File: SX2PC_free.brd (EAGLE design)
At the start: 20.3 x 26.8 mm, 5 parts

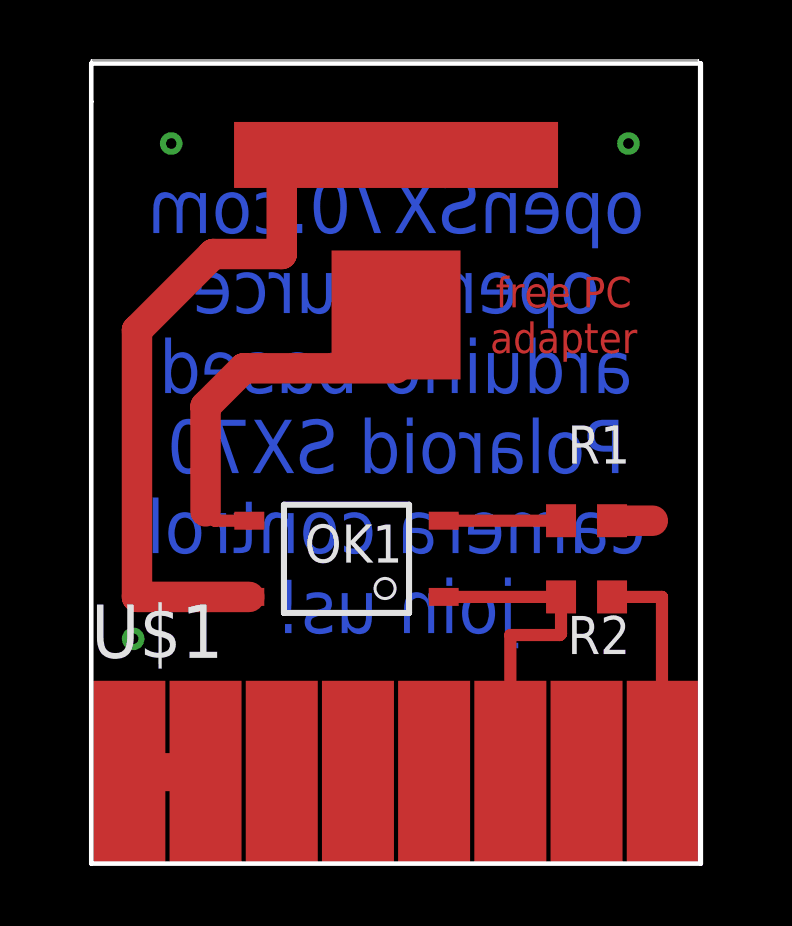
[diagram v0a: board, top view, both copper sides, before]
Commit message: Build a prototype and checked operation. Now working. Version 2.0
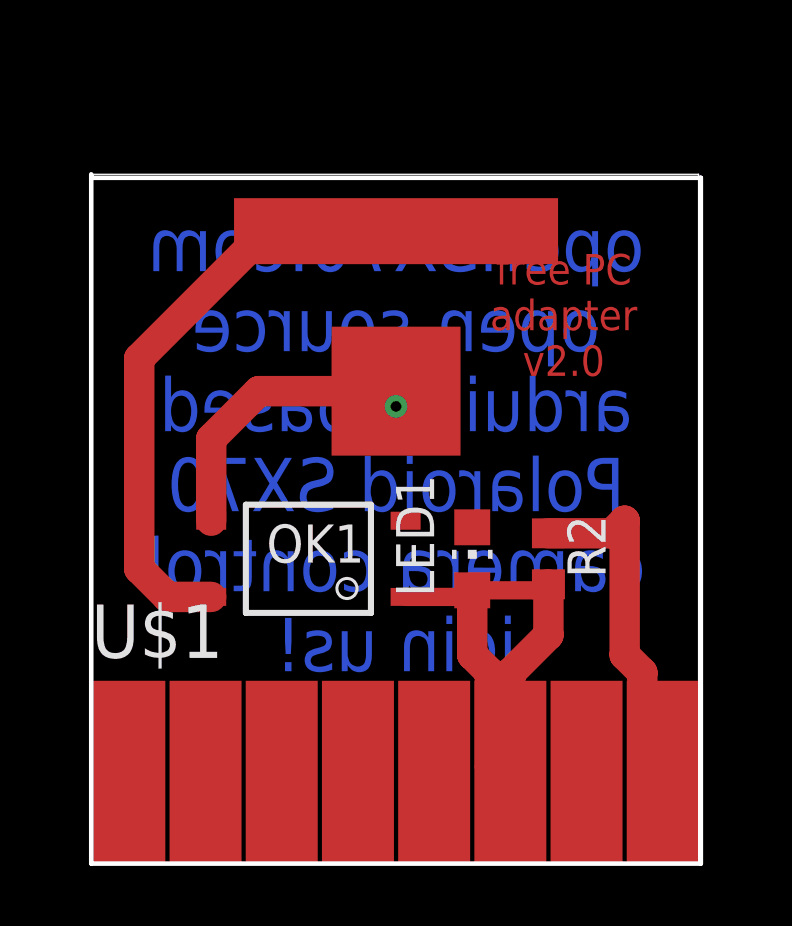
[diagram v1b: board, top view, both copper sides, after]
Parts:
- removed R1: 18R, rcl:R0603
- added LED1: (no value), led:CHIP-LED0805
- moved U$2 2.54 mm to (10.2, 19.1)
- moved R2 1.80 mm to (15.2, 10.2), turned to 90 degrees
- moved OK1 1.27 mm to (7.24, 9.53)
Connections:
- removed net N$2: OK1.2, R1.1
- net GND: now also LED1.C, OK1.2; no longer R1.2
- net N$3: now also LED1.A
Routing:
- net N$3: track 11.4 -> 19.2 mm
- net N$4: track 13.7 -> 9.55 mm
- net N$2: track 3.91 -> 0.00 mm
- net GND: track 8.87 -> 11.6 mm, vias 3 -> 0
- net N$1: track 2.54 -> 0.00 mm
- net N$5: track 25.2 -> 22.8 mm
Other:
- board size 20.3 x 26.8 mm -> 20.3 x 23 mm
- board text added: "free PC adapter v2.0"
- board text removed: "free PC adapter"
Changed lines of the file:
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@@
 <plain>
 <wire x1="0" y1="0" x2="20.244" y2="0" width="0" layer="20"/>
-<wire x1="20.244" y1="0" x2="20.244" y2="26.787" width="0" layer="20"/>
-<wire x1="20.244" y1="26.787" x2="0" y2="26.787" width="0" layer="20"/>
-<wire x1="0" y1="26.787" x2="0" y2="26.67" width="0" layer="20"/>
-<text x="10.16" y="15.24" size="1.778" layer="16" font="vector" ratio="16" rot="MR0" align="center">openSX70.com
+<wire x1="20.244" y1="0" x2="20.244" y2="22.977" width="0" layer="20"/>
+<wire x1="20.244" y1="22.977" x2="0" y2="22.977" width="0" layer="20"/>
+<text x="10.16" y="13.97" size="1.778" layer="16" font="vector" ratio="16" rot="MR0" align="center">openSX70.com
 open-source
 arduino-based
@@
 join us!</text>
 <text x="15.748" y="18.288" size="1.016" layer="1" font="vector" ratio="16" align="center">free PC
-adapter</text>
-<wire x1="0" y1="25.4" x2="0" y2="0" width="0.1524" layer="20"/>
+adapter
+v2.0</text>
+<wire x1="0" y1="22.977" x2="0" y2="22.86" width="0.1524" layer="20"/>
+<wire x1="0" y1="22.86" x2="0" y2="0" width="0.1524" layer="20"/>
 <wire x1="0" y1="0" x2="20.32" y2="0" width="0.1524" layer="20"/>
-<wire x1="20.32" y1="0" x2="20.32" y2="26.67" width="0.1524" layer="20"/>
-<wire x1="20.32" y1="26.67" x2="0" y2="26.67" width="0.1524" layer="20"/>
-<wire x1="0" y1="26.67" x2="0" y2="25.4" width="0.1524" layer="20"/>
+<wire x1="20.32" y1="0" x2="20.32" y2="22.86" width="0.1524" layer="20"/>
+<wire x1="20.32" y1="22.86" x2="0" y2="22.86" width="0.1524" layer="20"/>
 </plain>
 <attributes>
@@
 </autorouter>
 <elements>
-<element name="OK1" library="openSX70" package="SO-4" value="TLP127" x="8.509" y="9.525" smashed="yes" rot="R180">
-<attribute name="NAME" x="7.112" y="10.033" size="1.27" layer="25" font="vector" ratio="10"/>
-<attribute name="VALUE" x="5.588" y="12.446" size="1.27" layer="27" font="vector" ratio="10"/>
-</element>
-<element name="R1" library="rcl" library_urn="urn:adsk.eagle:library:334" package="R0603" package3d_urn="urn:adsk.eagle:package:23555/2" value="18R" x="16.51" y="11.43" smashed="yes">
-<attribute name="NAME" x="15.875" y="13.335" size="1.27" layer="25" font="vector"/>
-<attribute name="VALUE" x="18.415" y="10.795" size="1.27" layer="27"/>
+<element name="OK1" library="openSX70" package="SO-4" value="TLP127" x="7.239" y="9.525" smashed="yes" rot="R180">
+<attribute name="NAME" x="5.842" y="10.033" size="1.27" layer="25" font="vector" ratio="10"/>
+<attribute name="VALUE" x="4.318" y="12.446" size="1.27" layer="27" font="vector" ratio="10"/>
 </element>
 <element name="U$1" library="openSX70" package="SX70-FLASH-EDGE8" value="SX70-FLASH-EDGE8-MALE" x="10.16" y="3.048"/>
-<element name="U$2" library="openSX70" package="PC-SOCKET-KAISER-1311" value="PC-SOCKET-KAISER-1311" x="10.16" y="21.59"/>
-<element name="R2" library="rcl" library_urn="urn:adsk.eagle:library:334" package="R0603" package3d_urn="urn:adsk.eagle:package:23555/2" value="9R" x="16.51" y="8.89" smashed="yes">
-<attribute name="NAME" x="15.875" y="6.985" size="1.27" layer="25" font="vector"/>
-<attribute name="VALUE" x="18.415" y="8.255" size="1.27" layer="27" font="vector"/>
+<element name="U$2" library="openSX70" package="PC-SOCKET-KAISER-1311" value="PC-SOCKET-KAISER-1311" x="10.16" y="19.05"/>
+<element name="R2" library="rcl" library_urn="urn:adsk.eagle:library:334" package="R0603" package3d_urn="urn:adsk.eagle:package:23555/2" value="9R" x="15.24" y="10.16" smashed="yes" rot="R90">
+<attribute name="NAME" x="17.145" y="9.525" size="1.27" layer="25" font="vector" rot="R90"/>
+<attribute name="VALUE" x="15.875" y="12.065" size="1.27" layer="27" font="vector" rot="R90"/>
 </element>
+<element name="LED1" library="led" library_urn="urn:adsk.eagle:library:259" package="CHIP-LED0805" package3d_urn="urn:adsk.eagle:package:15818/1" value="" x="12.7" y="10.16"/>
 </elements>
 <signals>
@@
 <contactref element="U$1" pad="GND"/>
 <contactref element="U$1" pad="S2"/>
-<wire x1="1.27" y1="3.04926875" x2="3.81" y2="3.04926875" width="1.27" layer="1"/>
-</signal>
-<signal name="N$2">
-<contactref element="OK1" pad="2"/>
-<contactref element="R1" pad="1"/>
-<wire x1="11.749" y1="11.43" x2="15.66" y2="11.43" width="0.4064" layer="1"/>
+<wire x1="1.27" y1="3.04926875" x2="3.81" y2="3.04926875" width="0" layer="19" extent="1-1"/>
 </signal>
 <signal name="N$4">
 <contactref element="U$2" pad="TIP"/>
 <contactref element="OK1" pad="3"/>
-<wire x1="3.81" y1="15.24" x2="3.81" y2="11.74" width="1.016" layer="1"/>
-<wire x1="3.81" y1="15.24" x2="5.08" y2="16.51" width="1.016" layer="1"/>
-<wire x1="5.08" y1="16.51" x2="10.16" y2="16.51" width="1.016" layer="1"/>
-<wire x1="3.81" y1="11.74" x2="4.12" y2="11.43" width="0.4064" layer="1"/>
-<wire x1="4.12" y1="11.43" x2="5.269" y2="11.43" width="0.4064" layer="1"/>
-<wire x1="10.16" y1="16.51" x2="10.16" y2="18.288" width="0.4064" layer="1"/>
+<wire x1="3.999" y1="11.43" x2="3.999" y2="14.159" width="1.016" layer="1"/>
+<wire x1="5.588" y1="15.748" x2="10.16" y2="15.748" width="1.016" layer="1"/>
+<wire x1="3.999" y1="14.159" x2="5.588" y2="15.748" width="1.016" layer="1"/>
 </signal>
 <signal name="N$5">
 <contactref element="OK1" pad="4"/>
 <contactref element="U$2" pad="RING"/>
-<wire x1="5.269" y1="8.89" x2="1.524" y2="8.89" width="1.016" layer="1"/>
-<wire x1="1.524" y1="8.89" x2="1.524" y2="17.78" width="1.016" layer="1"/>
-<wire x1="1.524" y1="17.78" x2="4.064" y2="20.32" width="1.016" layer="1"/>
-<wire x1="4.064" y1="20.32" x2="6.35" y2="20.32" width="1.016" layer="1"/>
-<wire x1="6.35" y1="20.32" x2="6.35" y2="22.86" width="1.016" layer="1"/>
-<wire x1="6.35" y1="22.86" x2="7.112" y2="23.622" width="1.016" layer="1"/>
-<wire x1="7.112" y1="23.622" x2="10.16" y2="23.622" width="1.016" layer="1"/>
+<wire x1="3.999" y1="8.89" x2="2.54" y2="8.89" width="1.016" layer="1"/>
+<wire x1="2.54" y1="8.89" x2="1.6002" y2="9.8298" width="1.016" layer="1"/>
+<wire x1="6.0198" y1="21.2598" x2="11.43" y2="21.2598" width="1.016" layer="1"/>
+<wire x1="11.43" y1="21.2598" x2="11.2522" y2="21.082" width="1.016" layer="1"/>
+<wire x1="11.2522" y1="21.082" x2="10.16" y2="21.082" width="1.016" layer="1"/>
+<wire x1="1.6002" y1="9.8298" x2="1.6002" y2="16.8402" width="1.016" layer="1"/>
+<wire x1="1.6002" y1="16.8402" x2="6.0198" y2="21.2598" width="1.016" layer="1"/>
 </signal>
 <signal name="GND">
 <polygon width="0.508" layer="1" isolate="0.254">
-<vertex x="0" y="26.67"/>
-<vertex x="20.32" y="26.67"/>
+<vertex x="0" y="22.86"/>
+<vertex x="20.32" y="22.86"/>
 <vertex x="20.32" y="0"/>
 <vertex x="0" y="0"/>
 </polygon>
-<contactref element="R1" pad="2"/>
 <contactref element="U$1" pad="FLASH-1"/>
 <contactref element="R2" pad="2"/>
-<wire x1="17.36" y1="11.43" x2="18.72" y2="11.43" width="1.016" layer="1"/>
-<wire x1="17.36" y1="8.89" x2="19.0248" y2="8.89" width="0.4064" layer="1"/>
-<wire x1="19.0248" y1="8.89" x2="19.0248" y2="3.04926875" width="0.4064" layer="1"/>
-<via x="2.667" y="24.003" extent="1-16" drill="0.35"/>
 <polygon width="0.4064" layer="16">
-<vertex x="20.32" y="26.67"/>
+<vertex x="20.32" y="22.86"/>
 <vertex x="20.32" y="0"/>
 <vertex x="0" y="0"/>
-<vertex x="0" y="26.67"/>
+<vertex x="0" y="22.86"/>
 </polygon>
-<via x="1.397" y="7.493" extent="1-16" drill="0.35"/>
-<wire x1="19.0248" y1="3.04926875" x2="19.049996875" y2="3.04926875" width="0" layer="19" extent="1-1"/>
-<via x="17.907" y="24.003" extent="1-16" drill="0.35"/>
+<contactref element="OK1" pad="2"/>
+<contactref element="LED1" pad="C"/>
+<wire x1="15.24" y1="11.01" x2="17.36" y2="11.01" width="1.016" layer="1"/>
+<wire x1="17.36" y1="11.01" x2="17.78" y2="11.43" width="1.016" layer="1"/>
+<wire x1="18.3704" y1="6.3678125" x2="18.3704" y2="5.7596" width="1.016" layer="1"/>
+<wire x1="18.3704" y1="5.7596" x2="18.7198" y2="5.4102" width="1.016" layer="1"/>
+<wire x1="17.78" y1="11.43" x2="17.78" y2="6.9582125" width="1.016" layer="1"/>
+<wire x1="17.78" y1="6.9582125" x2="18.3704" y2="6.3678125" width="1.016" layer="1"/>
+<wire x1="18.7198" y1="5.4102" x2="18.7198" y2="3.379465625" width="1.016" layer="1"/>
+<wire x1="18.7198" y1="3.379465625" x2="19.049996875" y2="3.04926875" width="1.016" layer="1"/>
 </signal>
 <signal name="N$3">
@@
 <contactref element="U$1" pad="VCC-6V"/>
 <contactref element="R2" pad="1"/>
-<wire x1="11.749" y1="8.89" x2="15.66" y2="8.89" width="0.4064" layer="1"/>
-<wire x1="15.66" y1="8.89" x2="15.66" y2="7.659" width="0.4064" layer="1"/>
-<wire x1="15.66" y1="7.659" x2="15.621" y2="7.62" width="0.4064" layer="1"/>
-<wire x1="15.621" y1="7.62" x2="13.97" y2="7.62" width="0.4064" layer="1"/>
-<wire x1="13.97" y1="7.62" x2="13.97" y2="3.04926875" width="0.4064" layer="1"/>
+<contactref element="LED1" pad="A"/>
+<wire x1="15.24" y1="9.31" x2="15.24" y2="7.62" width="1.016" layer="1"/>
+<wire x1="15.24" y1="7.62" x2="13.97" y2="6.35" width="1.016" layer="1"/>
+<wire x1="13.97" y1="6.35" x2="13.97" y2="2.54" width="1.016" layer="1"/>
+<wire x1="13.97" y1="2.54" x2="13.2904" y2="3.2196" width="1.016" layer="1"/>
+<wire x1="13.2904" y1="3.2196" x2="13.2904" y2="6.3678125" width="1.016" layer="1"/>
+<wire x1="12.7" y1="8.89" x2="12.7" y2="6.9582125" width="1.016" layer="1"/>
+<wire x1="12.7" y1="8.89" x2="12.7" y2="9.11" width="1.016" layer="1"/>
+<wire x1="13.2904" y1="6.3678125" x2="12.7" y2="6.9582125" width="1.016" layer="1"/>
+<wire x1="10.479" y1="8.89" x2="12.7" y2="8.89" width="0.6096" layer="1"/>
+<wire x1="12.7" y1="9.11" x2="15.04" y2="9.11" width="0.6096" layer="1"/>
+<wire x1="15.04" y1="9.11" x2="15.24" y2="9.31" width="0.6096" layer="1"/>
+<wire x1="13.97" y1="2.54" x2="13.97" y2="3.04926875" width="0" layer="19" extent="1-1"/>
+</signal>
+<signal name="N$6">
+<via x="10.16" y="15.24" extent="1-16" drill="0.35" shape="square"/>
 </signal>
 </signals>

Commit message: Connected F1 and F5 to VCC or it doesn't work!
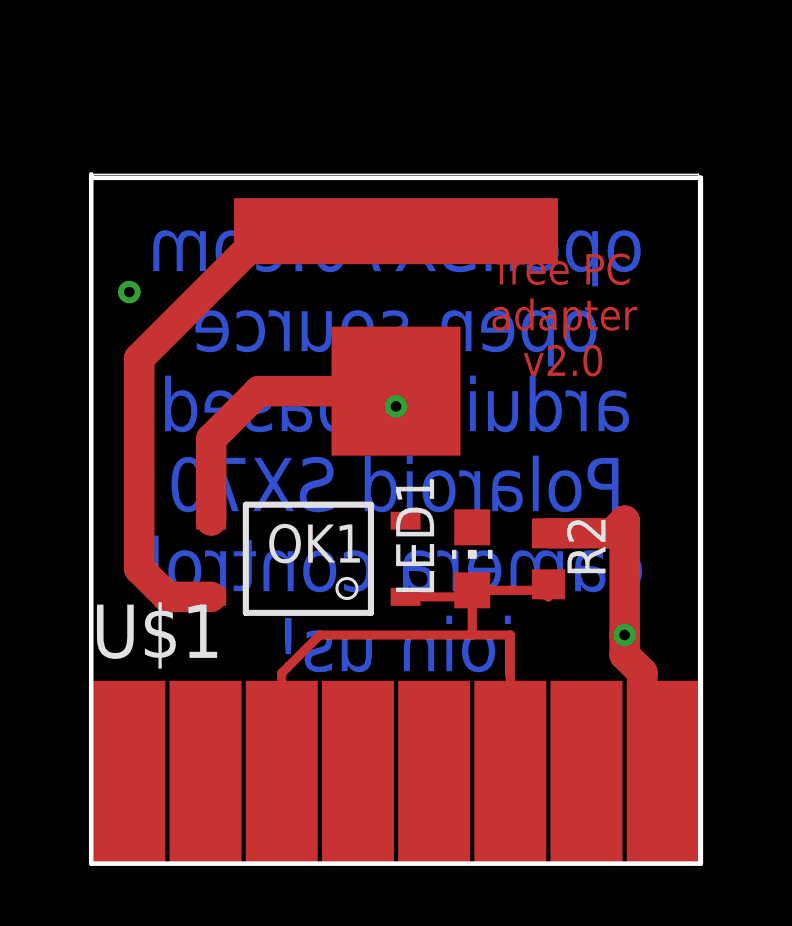
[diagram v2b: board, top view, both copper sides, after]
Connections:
- net N$3: now also U$1.FLASH-5
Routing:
- net N$3: track 19.2 -> 23.1 mm
- net GND: vias 0 -> 2
